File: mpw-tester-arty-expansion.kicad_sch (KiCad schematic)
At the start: 112 parts, among them J1 USB4105-GF-A, J10 61300211121, J11 61300211121, J12 61300211121, J14 61300311121, J15 61300311121, J18 61300411121, J19 61300711121, J20 61300411121, J3 Arty_A7_SPI, J4 61300211121, J5 61300311121, J6 61300211121, J7 61300211121, J8 61300211121, J9 61300211121, Q1 DTC014TEBTL, SW1 JS202011JCQN, U1 SN74LVC1G125DCKR, U2 FT232HQ, U3 SN74LVC1G125DCKR, U4 MAX811REUS+T, U5 NTS0102DP, U6 MCP4661-103E/ML, U7 Caravel_breakout_PCB, U8 W25Q32FVSS, U9 MIC2211-AAYML-TR, Y1 ABM8G-12.000MHZ-18-D2Y-T, Y2 ECS-2520MVLC-100-BN-TR

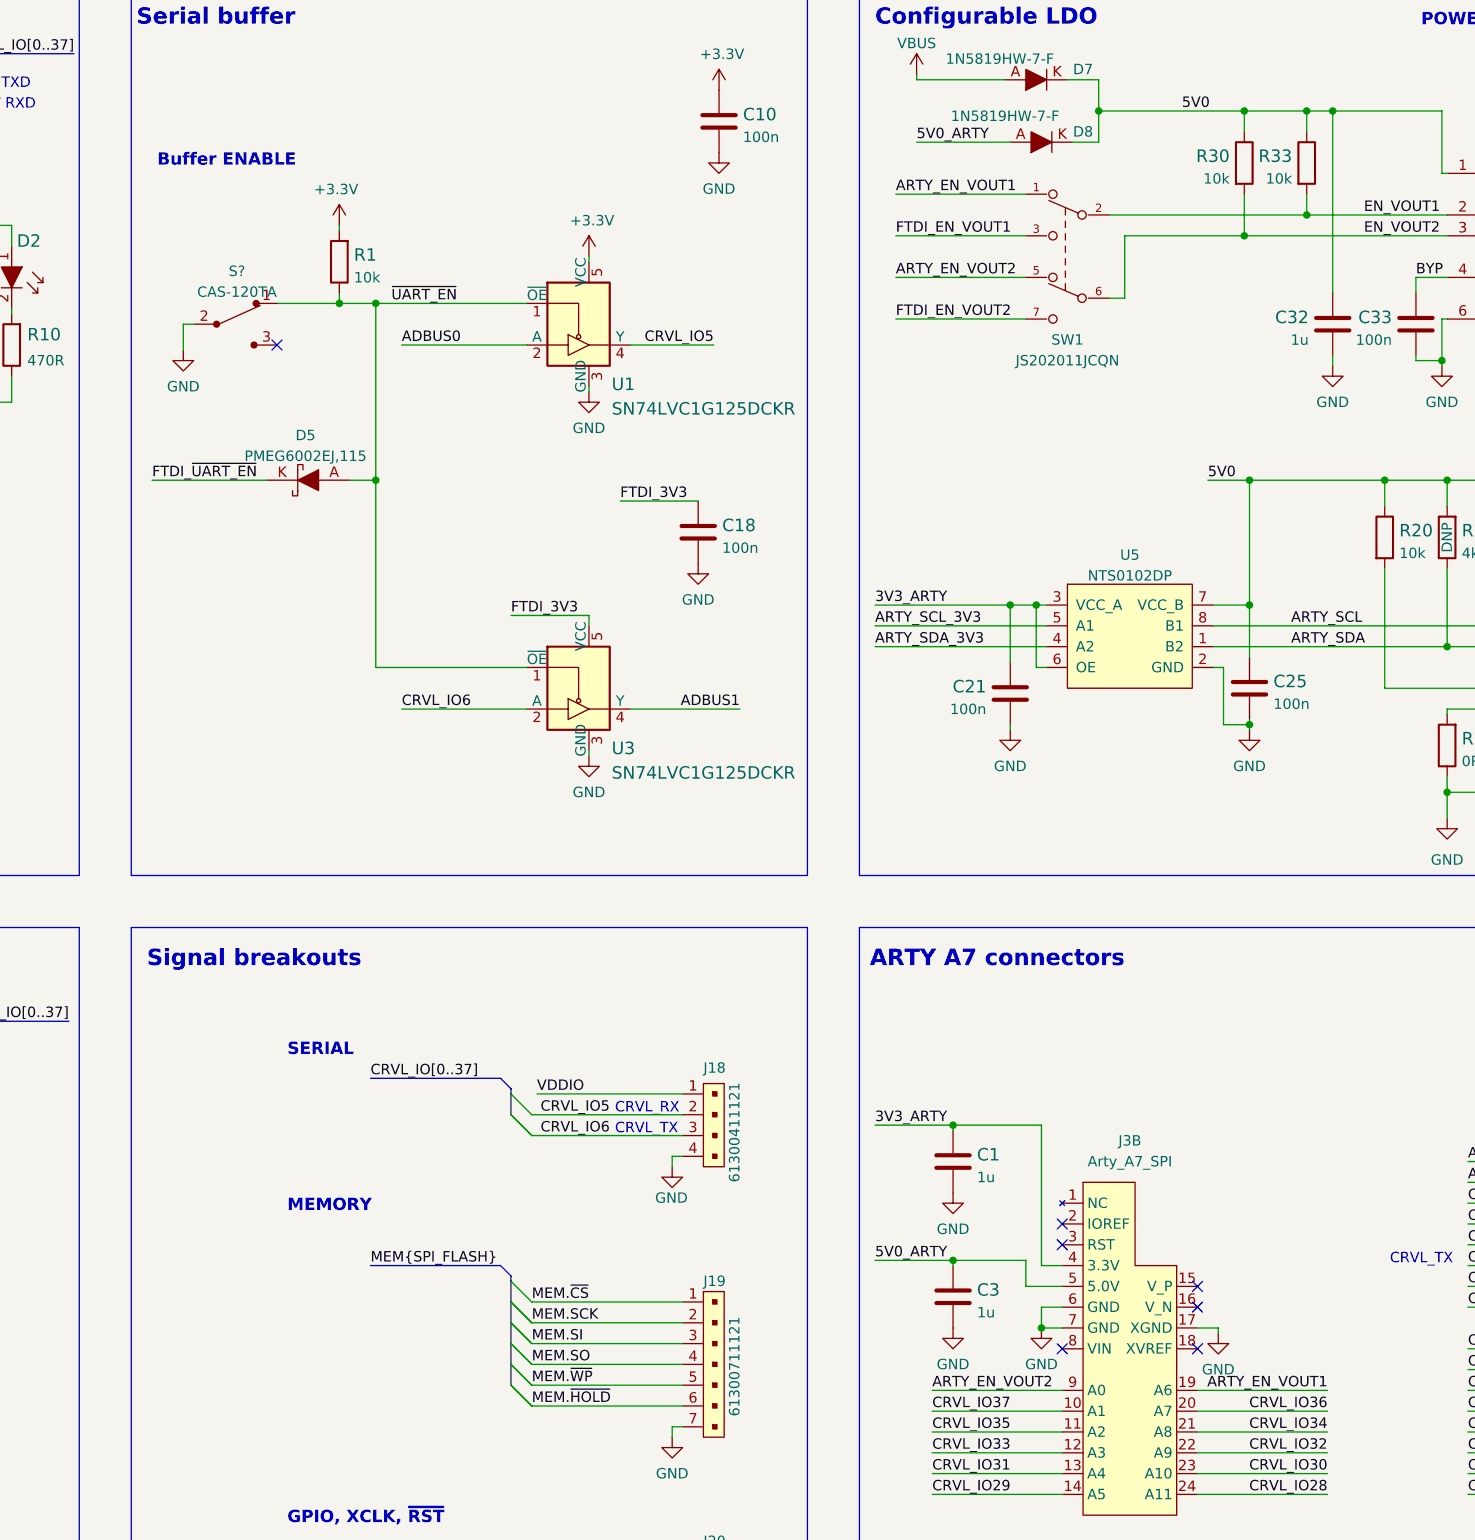
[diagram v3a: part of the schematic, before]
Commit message: Swap Arty_EN_VOUT 1 and 2. Continue layout
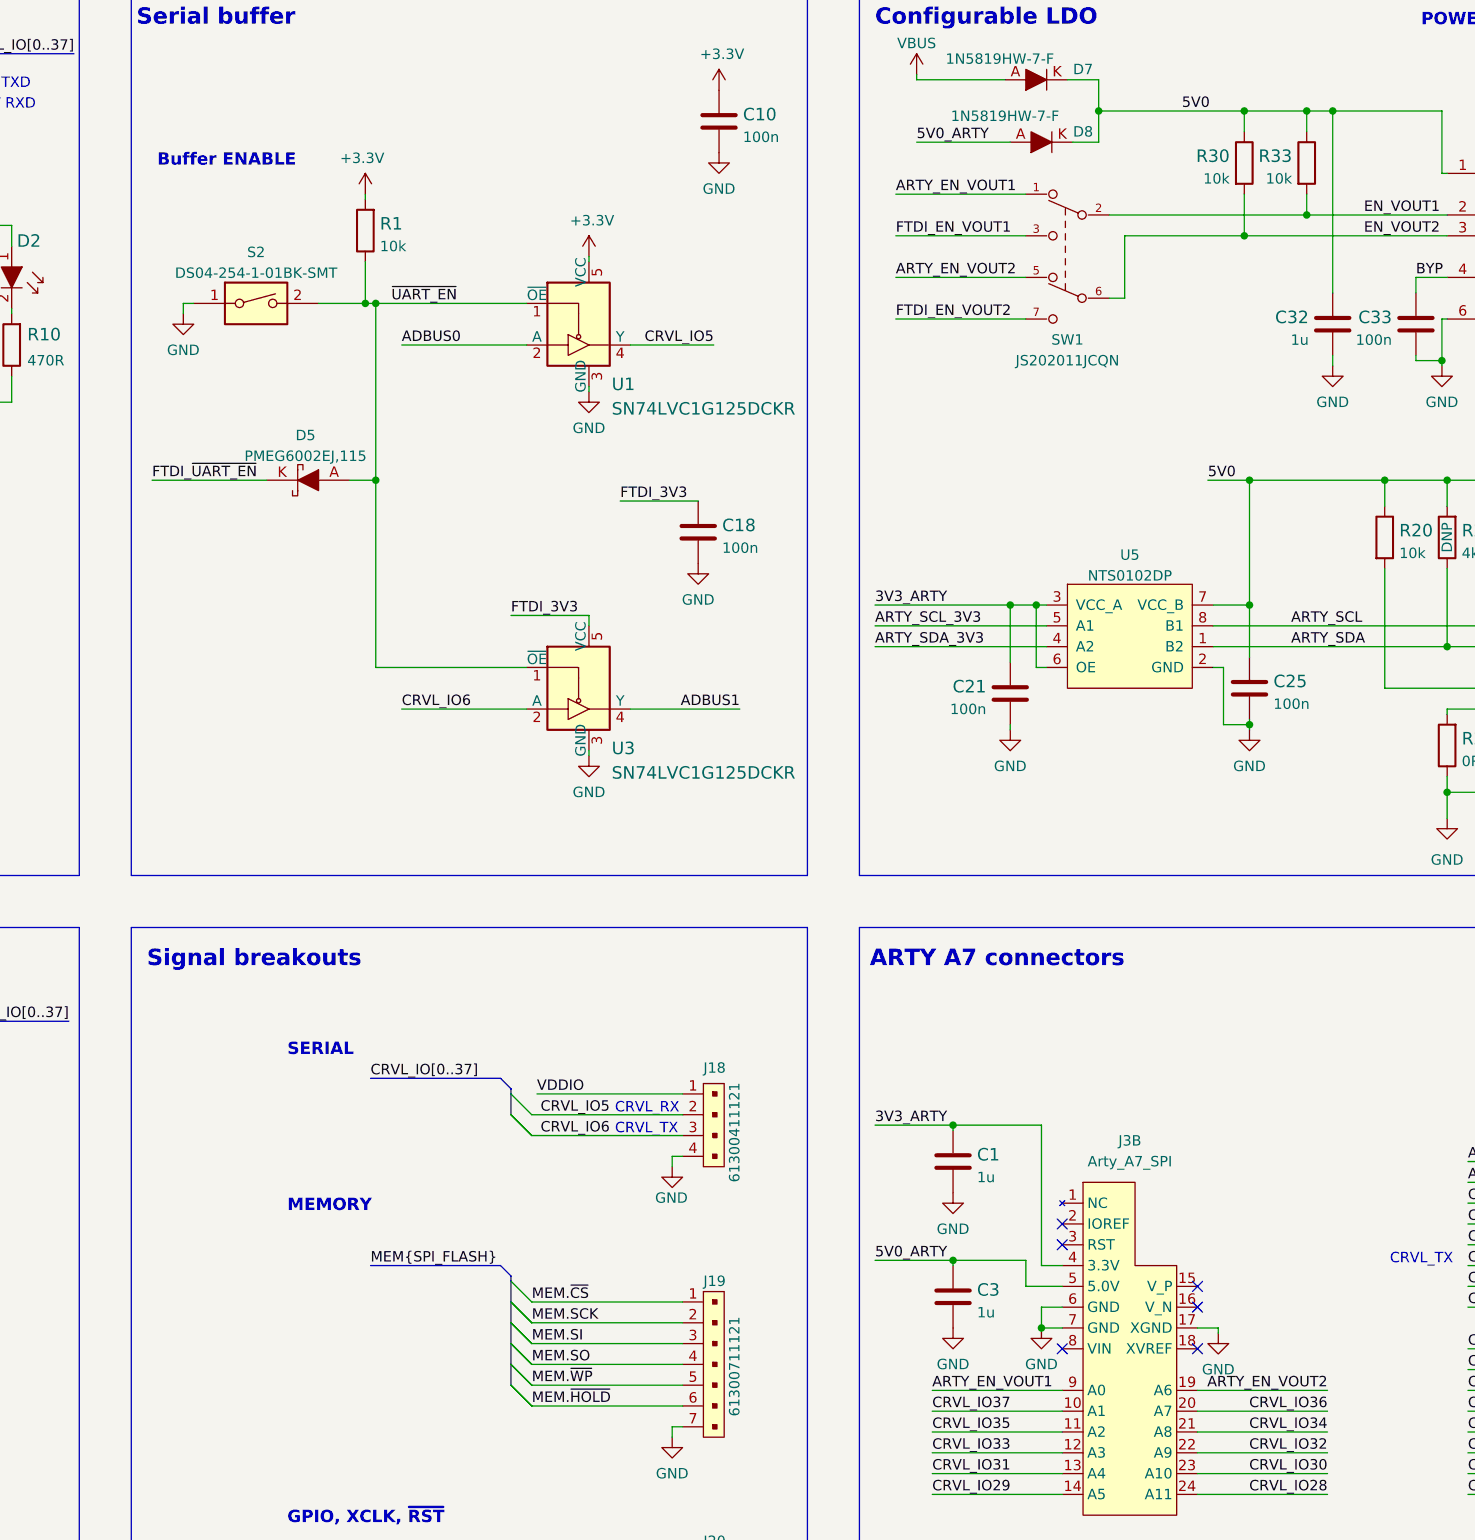
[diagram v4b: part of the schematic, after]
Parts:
- removed S?: CAS-120TA, antmicro-footprints:Switch_Slide_CAS-120TA, symbol antmicroSlideSwitches:CAS-120TA
- added S2: DS04-254-1-01BK-SMT, antmicro-footprints:SW_DS04-254-1-01BK-SMT, symbol antmicroSlideSwitches:DS04-254-1-01BK-SMT
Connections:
- net AGND: now also S2.1
- net ARTY_EN_VOUT1: now also J3.9 (A0); no longer J3.19 (A6)
- net ARTY_EN_VOUT2: now also J3.19 (A6); no longer J3.9 (A0)
- net ~{UART_EN}: now also S2.2
- no-connect marks 22 -> 21
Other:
- moved on the sheet: R1
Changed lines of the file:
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@@
   (junction (at 338.455 110.49) (diameter 0) (color 0 0 0 0)
   )
-  (junction (at 203.2 50.8) (diameter 0) (color 0 0 0 0)
-  )
   (junction (at 389.255 50.165) (diameter 0) (color 0 0 0 0)
   )
@@
   (junction (at 138.43 278.13) (diameter 0) (color 0 0 0 0)
   )
+  (junction (at 206.375 50.8) (diameter 0) (color 0 0 0 0)
+  )
   (junction (at 295.91 27.305) (diameter 0) (color 0 0 0 0)
   )
@@
   (no_connect (at 130.81 78.105))
   (no_connect (at 130.81 40.005))
-  (no_connect (at 195.58 55.88))
   (no_connect (at 291.465 165.735))
   (no_connect (at 130.81 75.565))
@@
     (stroke (width 0) (type default) (color 0 0 0 0))
   )
-  (wire (pts (xy 184.15 53.34) (xy 184.15 56.515))
+  (wire (pts (xy 184.15 50.8) (xy 184.15 52.07))
     (stroke (width 0) (type default) (color 0 0 0 0))
   )
@@
     (stroke (width 0) (type default) (color 0 0 0 0))
   )
-  (wire (pts (xy 203.2 41.275) (xy 203.2 41.91))
+  (wire (pts (xy 206.375 37.465) (xy 206.375 38.1))
     (stroke (width 0) (type default) (color 0 0 0 0))
   )
@@
     (stroke (width 0) (type default) (color 0 0 0 0))
   )
+  (wire (pts (xy 206.375 50.8) (xy 207.645 50.8))
+    (stroke (width 0) (type default) (color 0 0 0 0))
+  )
   (wire (pts (xy 134.62 208.915) (xy 150.495 208.915))
     (stroke (width 0) (type default) (color 0 0 0 0))
@@
     (stroke (width 0) (type default) (color 0 0 0 0))
   )
-  (wire (pts (xy 184.15 53.34) (xy 185.42 53.34))
-    (stroke (width 0) (type default) (color 0 0 0 0))
-  )
   (wire (pts (xy 130.81 32.385) (xy 151.13 32.385))
     (stroke (width 0) (type default) (color 0 0 0 0))
@@
     (stroke (width 0) (type default) (color 0 0 0 0))
   )
-  (wire (pts (xy 195.58 50.8) (xy 203.2 50.8))
-    (stroke (width 0) (type default) (color 0 0 0 0))
-  )
   (wire (pts (xy 219.71 254.635) (xy 219.71 255.27))
     (stroke (width 0) (type default) (color 0 0 0 0))
@@
     (stroke (width 0) (type default) (color 0 0 0 0))
   )
+  (wire (pts (xy 200.66 50.8) (xy 206.375 50.8))
+    (stroke (width 0) (type default) (color 0 0 0 0))
+  )
   (wire (pts (xy 135.255 278.13) (xy 138.43 278.13))
     (stroke (width 0) (type default) (color 0 0 0 0))
@@
     (stroke (width 0) (type default) (color 0 0 0 0))
   )
+  (wire (pts (xy 184.15 50.8) (xy 185.42 50.8))
+    (stroke (width 0) (type default) (color 0 0 0 0))
+  )
   (wire (pts (xy 34.925 259.715) (xy 34.925 260.985))
     (stroke (width 0) (type default) (color 0 0 0 0))
@@
     (stroke (width 0) (type default) (color 0 0 0 0))
   )
-  (wire (pts (xy 203.2 49.53) (xy 203.2 50.8))
+  (wire (pts (xy 206.375 45.72) (xy 206.375 50.8))
     (stroke (width 0) (type default) (color 0 0 0 0))
   )
@@
     (stroke (width 0) (type default) (color 0 0 0 0))
   )
-  (wire (pts (xy 203.2 50.8) (xy 207.645 50.8))
-    (stroke (width 0) (type default) (color 0 0 0 0))
-  )
   (wire (pts (xy 372.745 59.055) (xy 380.365 59.055))
     (stroke (width 0) (type default) (color 0 0 0 0))
@@
     (effects (font (size 1.27 1.27)) (justify right bottom))
   )
-  (label "ARTY_EN_VOUT1" (at 323.85 183.515 180)
-    (effects (font (size 1.27 1.27)) (justify right bottom))
+  (label "ARTY_EN_VOUT1" (at 275.59 183.515 0)
+    (effects (font (size 1.27 1.27)) (justify left bottom))
   )
   (label "CRVL_IO28" (at 138.43 213.995 0)
@@
     (effects (font (size 1.27 1.27)) (justify left bottom))
   )
-  (label "ARTY_EN_VOUT2" (at 275.59 183.515 0)
-    (effects (font (size 1.27 1.27)) (justify left bottom))
+  (label "ARTY_EN_VOUT2" (at 323.85 183.515 180)
+    (effects (font (size 1.27 1.27)) (justify right bottom))
   )
   (label "FTDI_3V3" (at 224.155 88.9 0)
@@
     (pin "8")
   )
-  (symbol (lib_id "antmicroSlideSwitches:CAS-120TA") (at 190.5 53.34 0) (unit 1)
-    (in_bom yes) (on_board yes) (fields_autoplaced)
-    (property "Reference" "S?" (id 0) (at 190.7032 46.8716 0))
-    (property "Value" "CAS-120TA" (id 1) (at 190.7032 49.4085 0))
-    (property "Footprint" "antmicro-footprints:Switch_Slide_CAS-120TA" (id 2) (at 195.58 48.26 0)
-      (effects (font (size 1.27 1.27)) (justify left) hide)
-    )
-    (property "Datasheet" "" (id 3) (at 195.58 45.72 0)
-      (effects (font (size 1.524 1.524)) (justify left) hide)
-    )
-    (property "MPN" "CAS-120TA" (id 4) (at 195.58 40.64 0)
-      (effects (font (size 1.524 1.524)) (justify left) hide)
-    )
-    (property "Manufacturer" "Nidec" (id 5) (at 195.58 37.592 0)
-      (effects (font (size 1.524 1.524)) (justify left) hide)
-    )
-    (pin "1")
-    (pin "2")
-    (pin "3")
-  )
   (symbol (lib_id "power:GND") (at 32.385 111.125 0) (unit 1)
     (in_bom yes) (on_board yes) (fields_autoplaced)
@@
     (pin "1")
   )
-  (symbol (lib_id "power:+3.3V") (at 203.2 41.275 0) (mirror y) (unit 1)
+  (symbol (lib_id "power:+3.3V") (at 206.375 37.465 0) (mirror y) (unit 1)
     (in_bom yes) (on_board yes)
-    (property "Reference" "#PWR0156" (id 0) (at 203.2 45.085 0)
+    (property "Reference" "#PWR0156" (id 0) (at 206.375 41.275 0)
       (effects (font (size 1.27 1.27)) hide)
     )
-    (property "Value" "+3.3V" (id 1) (at 202.819 36.8808 0))
-    (property "Footprint" "" (id 2) (at 203.2 41.275 0)
+    (property "Value" "+3.3V" (id 1) (at 205.994 33.0708 0))
+    (property "Footprint" "" (id 2) (at 206.375 37.465 0)
       (effects (font (size 1.27 1.27)) hide)
     )
-    (property "Datasheet" "" (id 3) (at 203.2 41.275 0)
+    (property "Datasheet" "" (id 3) (at 206.375 37.465 0)
       (effects (font (size 1.27 1.27)) hide)
     )
@@
     (pin "2")
   )
-  (symbol (lib_id "power:GND") (at 184.15 56.515 0) (mirror y) (unit 1)
+  (symbol (lib_id "power:GND") (at 184.15 52.07 0) (mirror y) (unit 1)
     (in_bom yes) (on_board yes) (fields_autoplaced)
-    (property "Reference" "#PWR0152" (id 0) (at 184.15 62.865 0)
+    (property "Reference" "#PWR0152" (id 0) (at 184.15 58.42 0)
       (effects (font (size 1.27 1.27)) hide)
     )
-    (property "Value" "GND" (id 1) (at 184.15 60.96 0))
-    (property "Footprint" "" (id 2) (at 184.15 56.515 0)
+    (property "Value" "GND" (id 1) (at 184.15 56.515 0))
+    (property "Footprint" "" (id 2) (at 184.15 52.07 0)
       (effects (font (size 1.27 1.27)) hide)
     )
-    (property "Datasheet" "" (id 3) (at 184.15 56.515 0)
+    (property "Datasheet" "" (id 3) (at 184.15 52.07 0)
       (effects (font (size 1.27 1.27)) hide)
     )
@@
     (pin "1")
   )
-  (symbol (lib_id "antmicroResistors0603:R_10k_0603") (at 203.2 45.72 90) (unit 1)
+  (symbol (lib_id "antmicroResistors0603:R_10k_0603") (at 206.375 41.91 90) (unit 1)
     (in_bom yes) (on_board yes) (fields_autoplaced)
-    (property "Reference" "R1" (id 0) (at 204.978 44.8854 90)
+    (property "Reference" "R1" (id 0) (at 208.153 41.0754 90)
       (effects (font (size 1.524 1.524)) (justify right))
     )
-    (property "Value" "R_10k_0603" (id 1) (at 207.01 45.72 0)
+    (property "Value" "R_10k_0603" (id 1) (at 210.185 41.91 0)
       (effects (font (size 1.524 1.524)) hide)
     )
-    (property "Footprint" "antmicro-footprints:0603-res" (id 2) (at 198.12 40.64 0)
+    (property "Footprint" "antmicro-footprints:0603-res" (id 2) (at 201.295 36.83 0)
       (effects (font (size 1.524 1.524)) (justify left) hide)
     )
-    (property "Datasheet" "" (id 3) (at 203.2 45.72 0)
+    (property "Datasheet" "" (id 3) (at 206.375 41.91 0)
       (effects (font (size 1.27 1.27)) hide)
     )
-    (property "Manufacturer" "BOURNS" (id 4) (at 193.04 40.64 0)
+    (property "Manufacturer" "BOURNS" (id 4) (at 196.215 36.83 0)
       (effects (font (size 1.524 1.524)) (justify left) hide)
     )
-    (property "MPN" "CR0603-JW-103ELF" (id 5) (at 195.58 40.64 0)
+    (property "MPN" "CR0603-JW-103ELF" (id 5) (at 198.755 36.83 0)
       (effects (font (size 1.524 1.524)) (justify left) hide)
     )
-    (property "Val" "10k" (id 6) (at 204.978 47.6505 90)
+    (property "Val" "10k" (id 6) (at 208.153 43.8405 90)
       (effects (font (size 1.27 1.27)) (justify right))
     )
@@
     (pin "1")
   )
+  (symbol (lib_id "antmicroSlideSwitches:DS04-254-1-01BK-SMT") (at 193.04 50.8 0) (unit 1)
+    (in_bom yes) (on_board yes) (fields_autoplaced)
+    (property "Reference" "S2" (id 0) (at 193.04 44.5602 0))
+    (property "Value" "DS04-254-1-01BK-SMT" (id 1) (at 193.04 47.0971 0))
+    (property "Footprint" "antmicro-footprints:SW_DS04-254-1-01BK-SMT" (id 2) (at 207.01 64.77 0)
+      (effects (font (size 1.27 1.27)) hide)
+    )
+    (property "Datasheet" "https://www.mouser.pl/datasheet/2/670/ds04_254_smt-1777718.pdf" (id 3) (at 217.17 62.23 0)
+      (effects (font (size 1.27 1.27)) hide)
+    )
+    (property "MPN" "DS04-254-1-01BK-SMT" (id 4) (at 194.31 59.69 0)
+      (effects (font (size 1.27 1.27)) hide)
+    )
+    (property "Manufacturer" "CUI Devices" (id 5) (at 186.69 57.15 0)
+      (effects (font (size 1.27 1.27)) hide)
+    )
+    (pin "1")
+    (pin "2")
+  )
   (symbol (lib_id "antmicroCapacitors0603:C_1u_0603") (at 278.13 172.085 0) (unit 1)
     (in_bom yes) (on_board yes) (fields_autoplaced)
@@
       (reference "S1") (unit 1) (value "KMR2") (footprint "antmicro-footprints:SW_SPST_4.2x2.8")
     )
-    (path "/0181eb65-882c-4f95-925a-a06f749f720f"
-      (reference "S?") (unit 1) (value "CAS-120TA") (footprint "antmicro-footprints:Switch_Slide_CAS-120TA")
+    (path "/a836baa3-8ac2-4847-af0a-a111152cf334"
+      (reference "S2") (unit 1) (value "DS04-254-1-01BK-SMT") (footprint "antmicro-footprints:SW_DS04-254-1-01BK-SMT")
     )
     (path "/217fd962-074c-4916-811c-40f9b3ccfd63"
